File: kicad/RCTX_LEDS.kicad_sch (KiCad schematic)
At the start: 51 parts

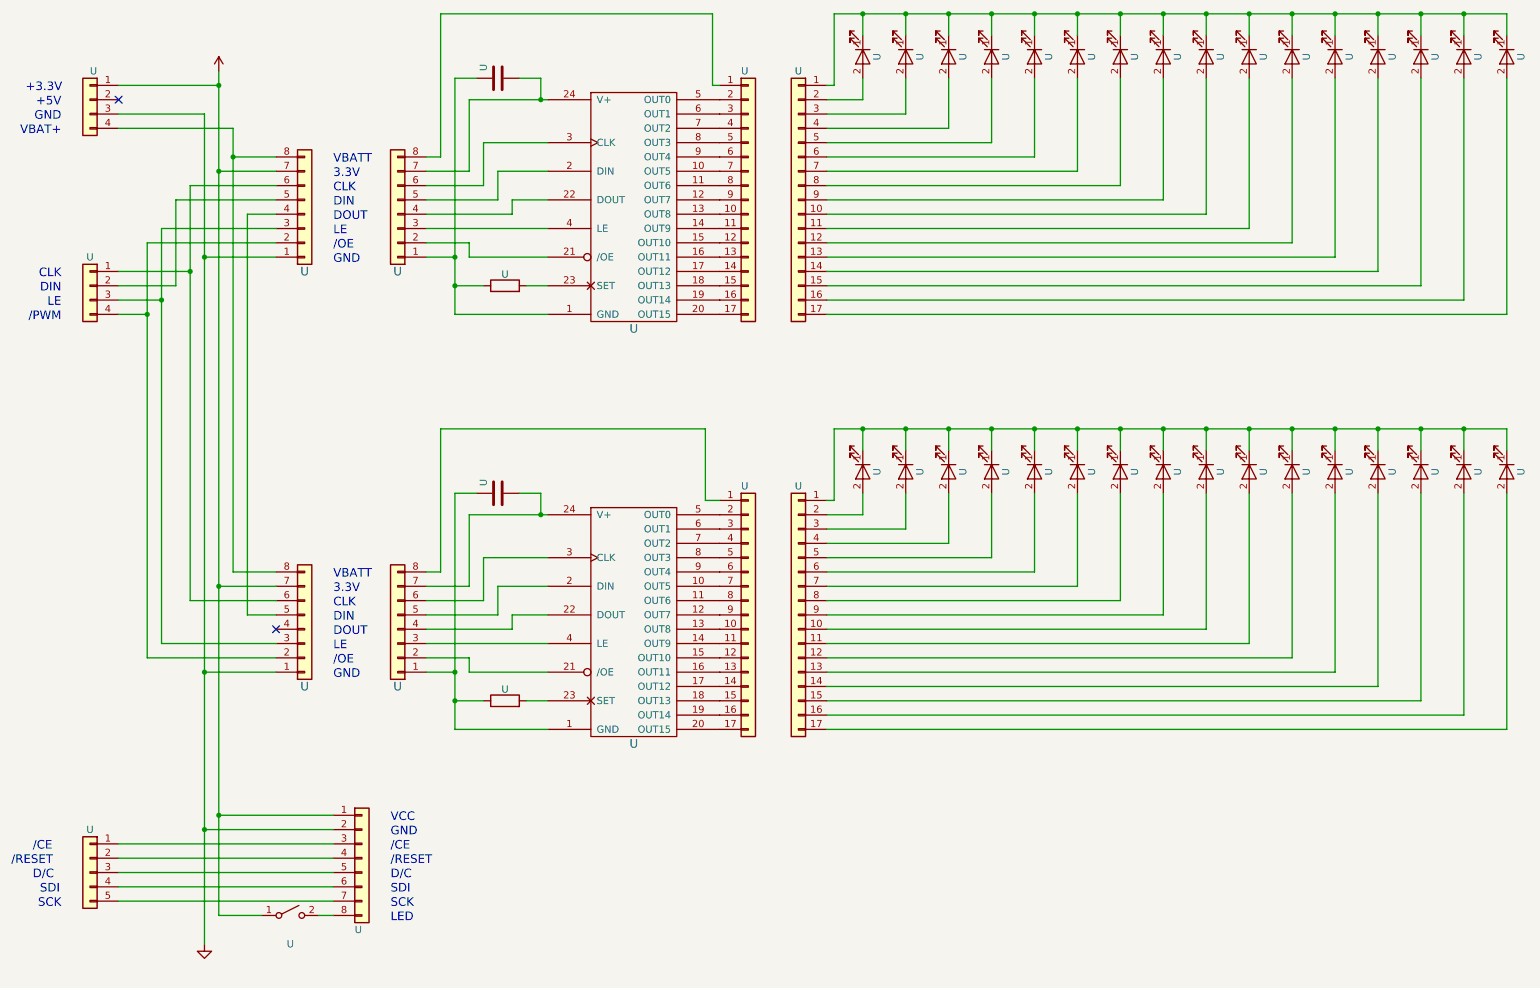
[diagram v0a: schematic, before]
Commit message: Adding PIB USB BRIDGE UML state diagrams - WIP
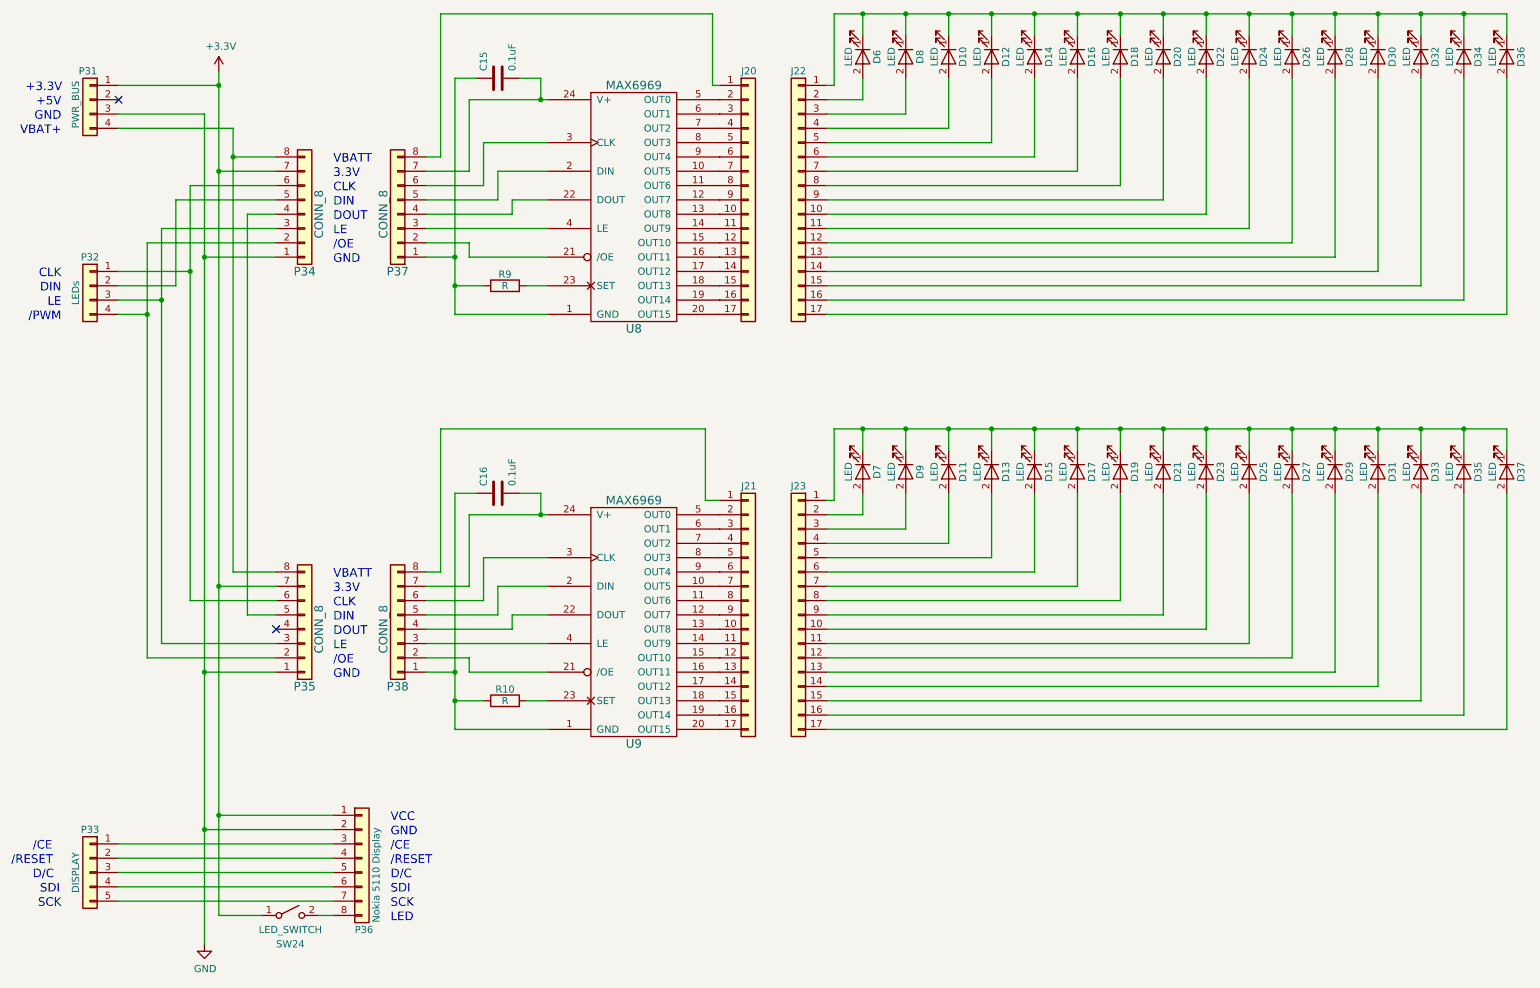
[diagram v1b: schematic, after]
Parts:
- C15, C16: renamed from U; value (none) -> 0.1uF; footprint (none) -> Capacitors_THT:C_Disc_D3.0mm_W1.6mm_P2.50mm
- D10, D11, D12, D13, D14, D15, D16, D17, D18, D19, D20, D21, D22, D23, D24, D25, D26, D27, D28, D29, D30, D31, D32, D33, D34, D35, D36, D37, D6, D7, D8, D9: renamed from U; value (none) -> LED; footprint (none) -> LEDs:LED_D2.0mm_W4.0mm_H2.8mm_FlatTop
- J20, J21, J22, J23: renamed from U; value (none) -> Conn_01x17; footprint (none) -> Connectors_Samtec:SL-117-X-XX_1x17
- P31: renamed from U; value (none) -> PWR_BUS; footprint (none) -> Connectors_Samtec:SL-104-X-XX_1x04
- P32: renamed from U; value (none) -> LEDs; footprint (none) -> Connectors_Samtec:SL-104-X-XX_1x04
- P33: renamed from U; value (none) -> DISPLAY; footprint (none) -> Connectors_Samtec:SL-105-X-XX_1x05
- P34, P35, P37, P38: renamed from U; value (none) -> CONN_8; footprint (none) -> Connectors_Samtec:SL-108-X-XX_1x08
- P36: renamed from U; value (none) -> Nokia 5110 Display; footprint (none) -> Connectors_Samtec:SL-108-X-XX_1x08
- R10, R9: renamed from U; value (none) -> R; footprint (none) -> Resistors_THT:R_Axial_DIN0204_L3.6mm_D1.6mm_P1.90mm_Vertical
- SW24: renamed from U; value (none) -> LED_SWITCH; footprint (none) -> Buttons_Switches_THT:SW_DIP_x1_W7.62mm_Slide_LowProfile
- U8, U9: renamed from U; value (none) -> MAX6969; footprint (none) -> Housings_DIP:DIP-24_W7.62mm
